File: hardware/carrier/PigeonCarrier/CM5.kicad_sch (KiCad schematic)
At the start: 3 parts, among them J1 10164227-1001A1RLF, J2 10164227-1001A1RLF

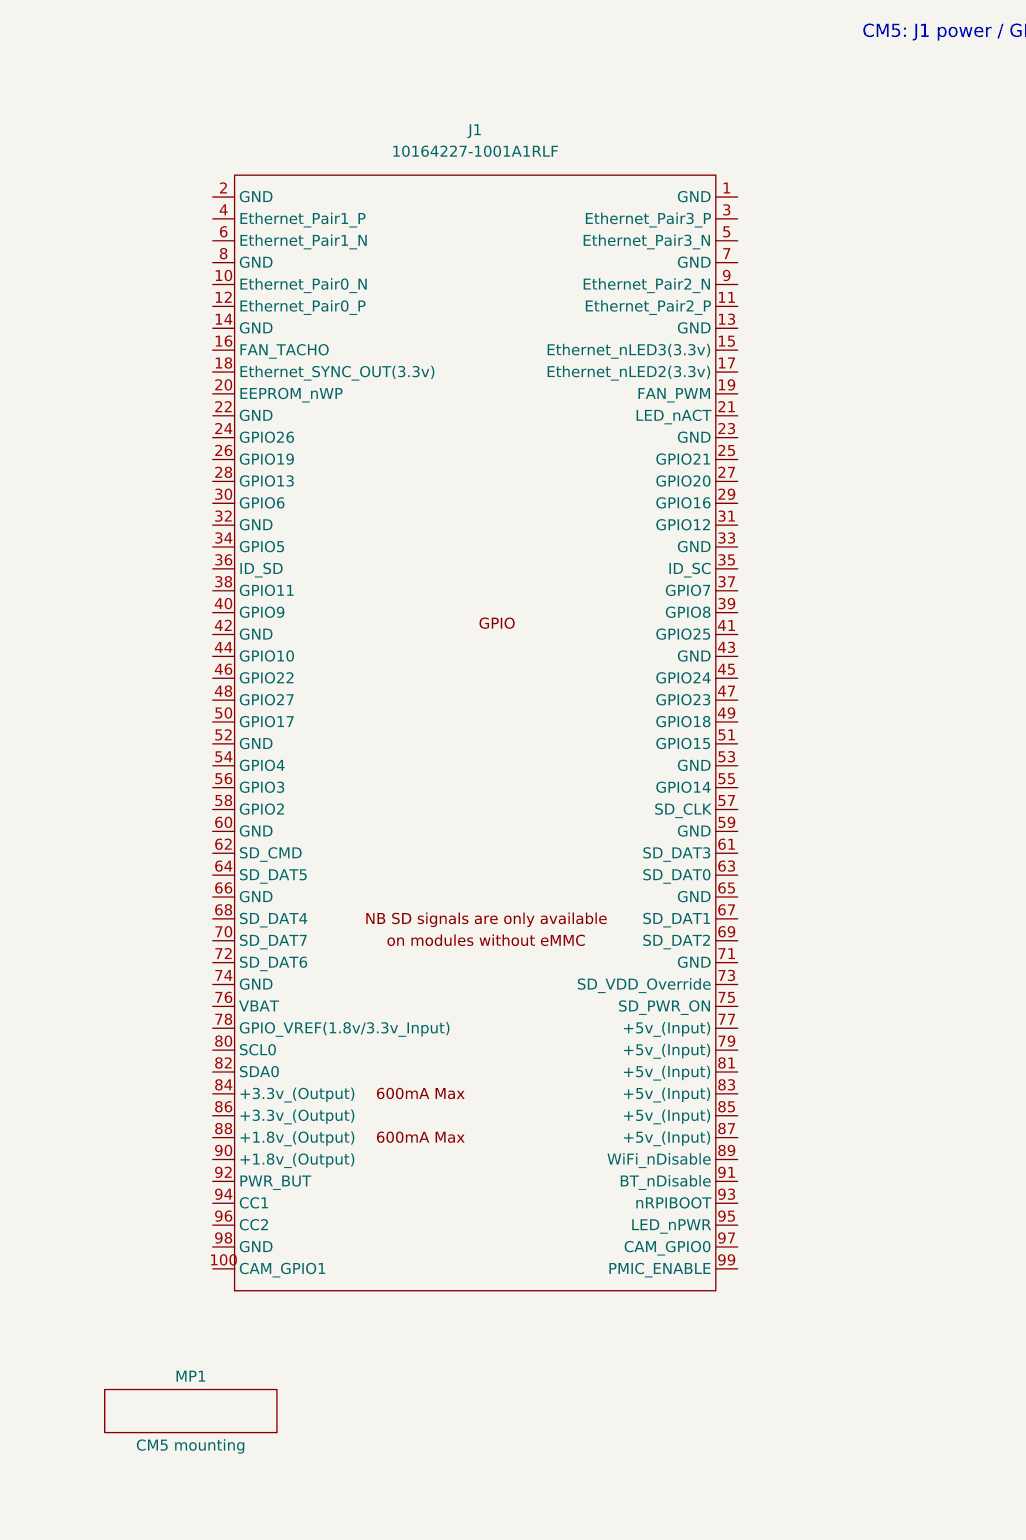
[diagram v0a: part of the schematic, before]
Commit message: shortned readmes + start of power stuff
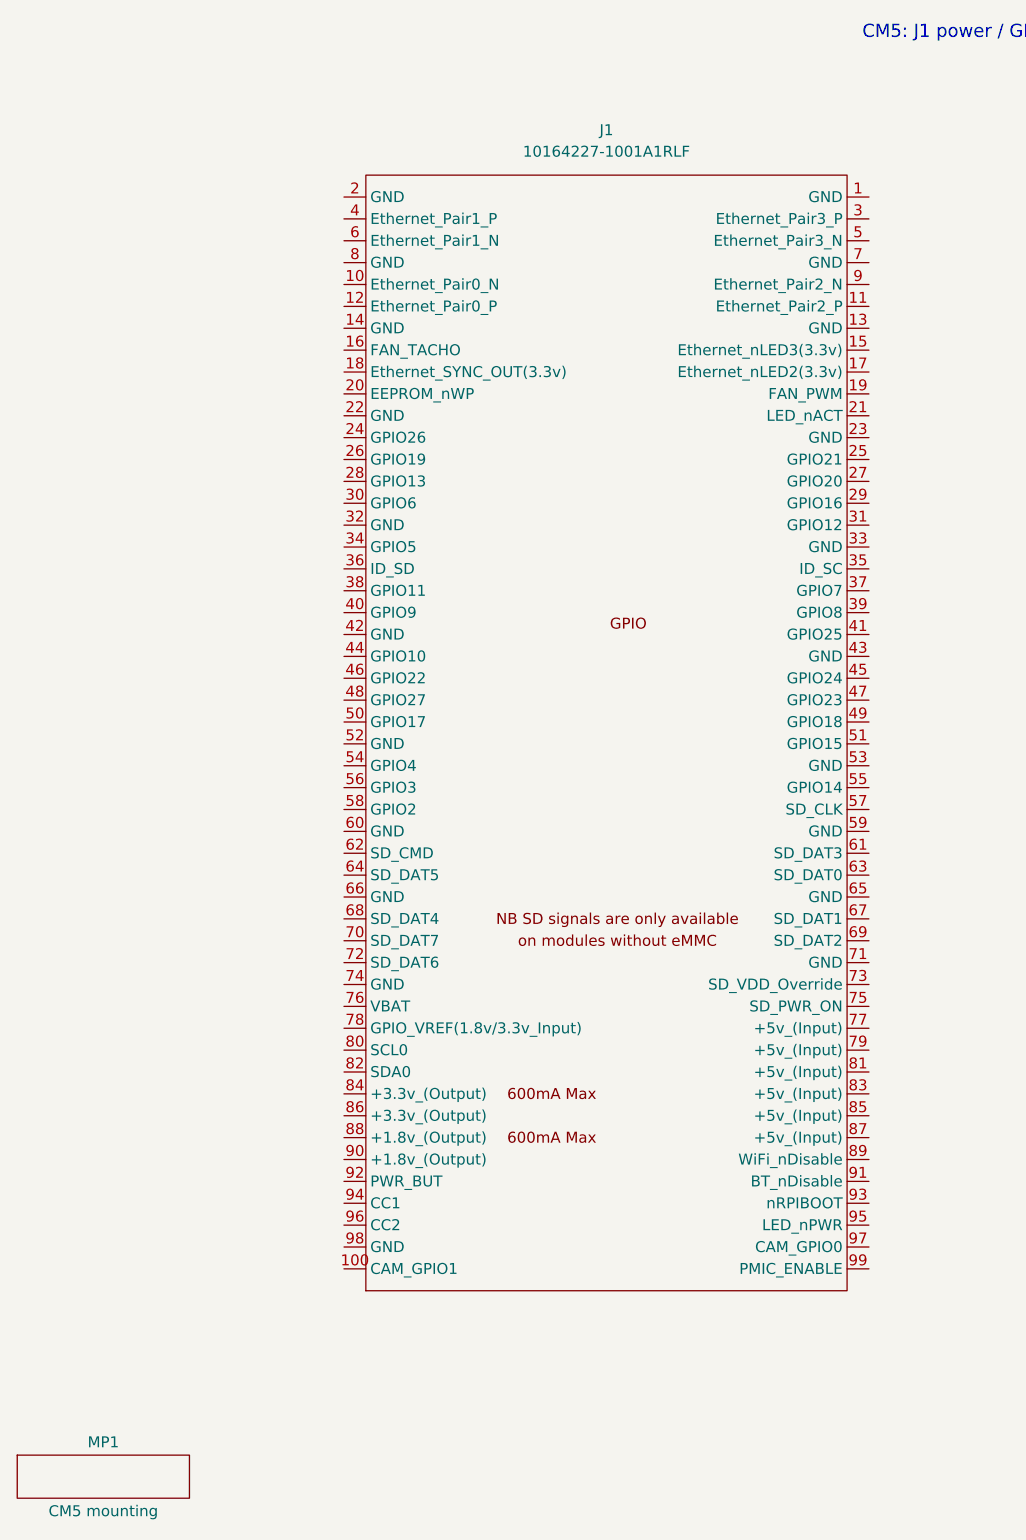
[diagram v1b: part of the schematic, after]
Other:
- moved on the sheet: J1, MP1

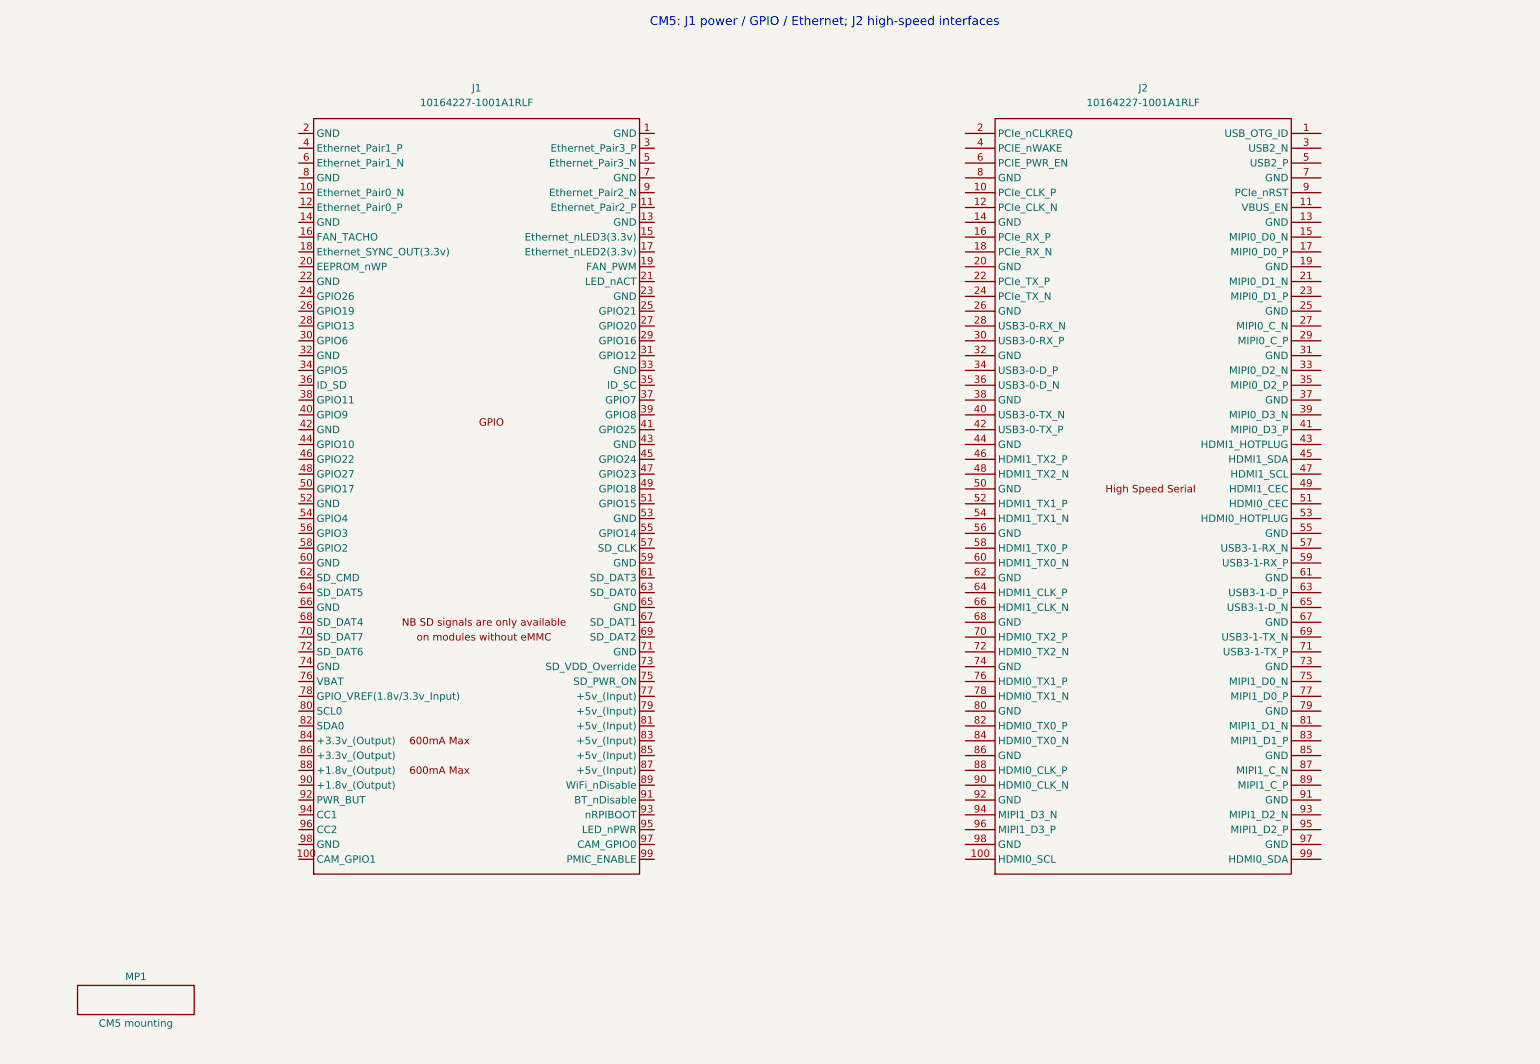
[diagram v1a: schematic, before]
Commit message: Update carrier schematics, parts library, and JLC rules
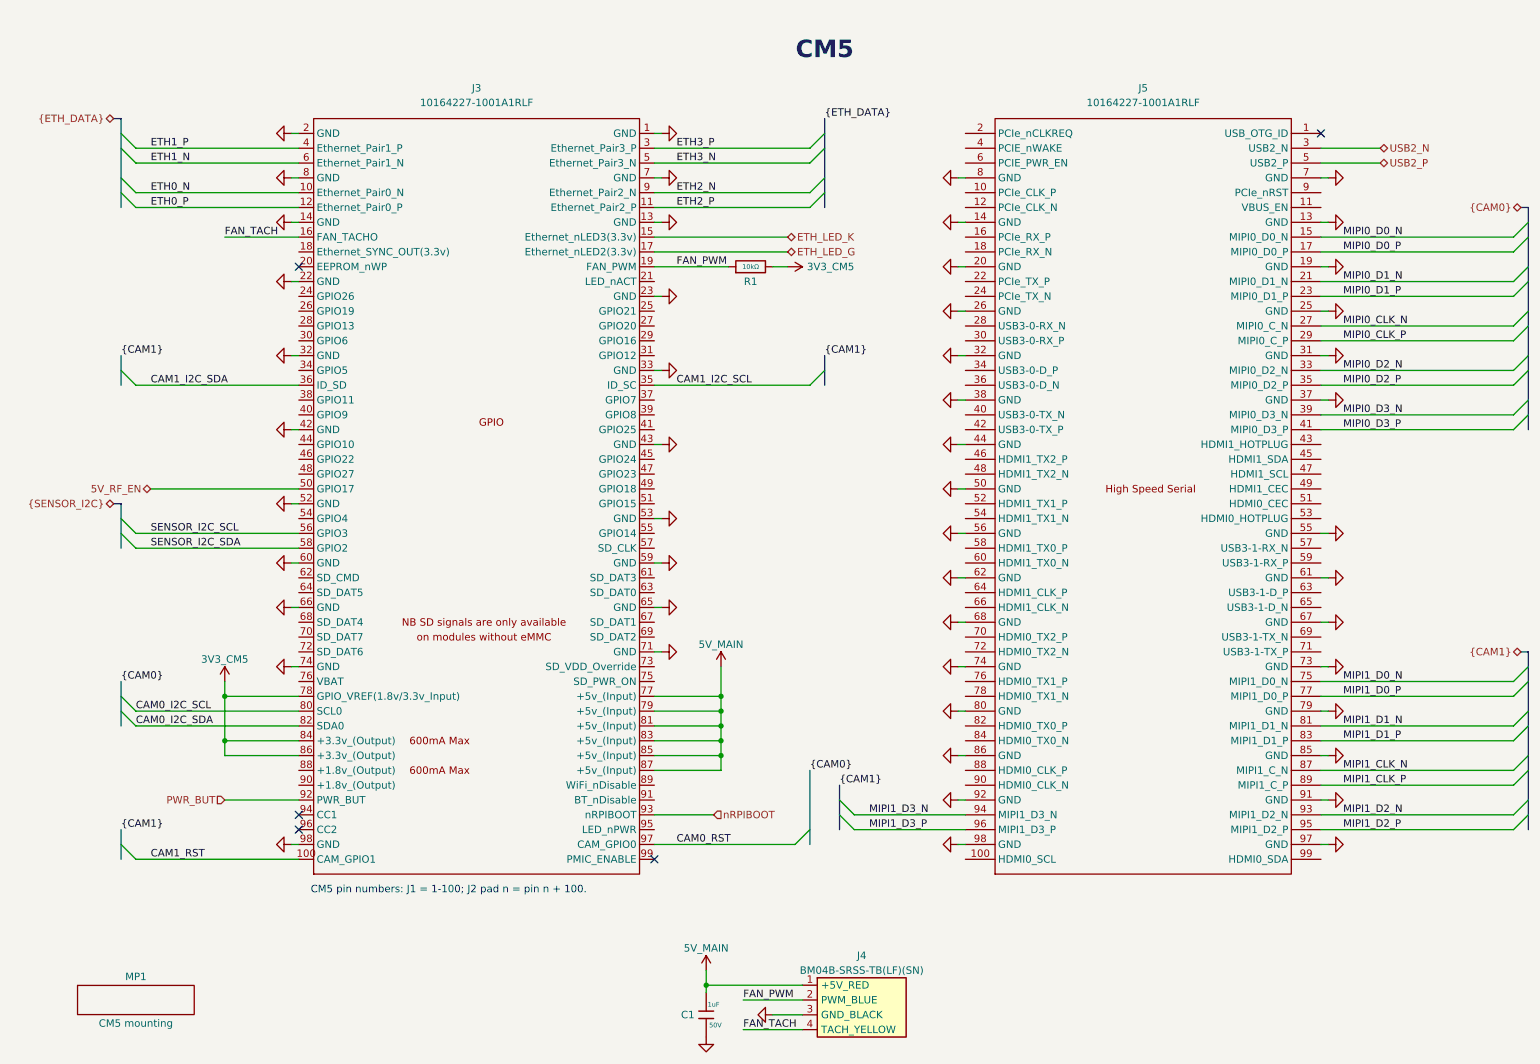
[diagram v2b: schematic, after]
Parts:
- added C1: 1uF, PCM_JLCPCB:C_0805, symbol PCM_JLCPCB-Capacitors:0805,1uF
- added J4: BM04B-SRSS-TB(LF)(SN), PigeonVision:JST_SH_BM04B-SRSS-TB_1x04-1MP_P1.00mm_Vertical, symbol PigeonVision:CM5_Fan_BM04B_SRSS_TB
- added R1: 10kΩ, PCM_JLCPCB:R_0402, symbol PCM_JLCPCB-Resistors:0402,10kΩ
- renumbered J1 to J3, J2 to J5
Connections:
- net GND: now reaches J5.13 (GND)
- net GND: now also J3.1 (GND), J3.13 (GND), J3.14 (GND), J3.2 (GND), J3.22 (GND), J3.23 (GND), J3.32 (GND), J3.33 (GND), J3.42 (GND), J3.43 (GND), J3.52 (GND), J3.53 (GND), J3.59 (GND), J3.60 (GND), J3.65 (GND), J3.66 (GND), J3.7 (GND), J3.71 (GND), J3.74 (GND), J3.8 (GND), J3.98 (GND), J5.14 (GND), J5.19 (GND), J5.20 (GND), J5.25 (GND), J5.26 (GND), J5.31 (GND), J5.32 (GND), J5.37 (GND), J5.38 (GND), J5.44 (GND), J5.50 (GND), J5.55 (GND), J5.56 (GND), J5.61 (GND), J5.62 (GND), J5.67 (GND), J5.68 (GND), J5.7 (GND), J5.73 (GND), J5.74 (GND), J5.79 (GND), J5.8 (GND), J5.80 (GND), J5.85 (GND), J5.86 (GND), J5.91 (GND), J5.92 (GND), J5.97 (GND), J5.98 (GND), C1.2, J4.3 (GND_BLACK)
- net MIPI0_D0_N: now reaches J5.15 (MIPI0_D0_N)
- net MIPI0_D0_P: now reaches J5.17 (MIPI0_D0_P)
- net MIPI0_D1_N: now reaches J5.21 (MIPI0_D1_N)
- net MIPI0_D1_P: now reaches J5.23 (MIPI0_D1_P)
- net MIPI0_CLK_N: now reaches J5.27 (MIPI0_C_N)
- net MIPI0_CLK_P: now reaches J5.29 (MIPI0_C_P)
- net USB2_N: now reaches J5.3 (USB2_N)
- net MIPI0_D2_N: now reaches J5.33 (MIPI0_D2_N)
- net MIPI0_D2_P: now reaches J5.35 (MIPI0_D2_P)
- net MIPI0_D3_N: now reaches J5.39 (MIPI0_D3_N)
- net MIPI0_D3_P: now reaches J5.41 (MIPI0_D3_P)
- net USB2_P: now reaches J5.5 (USB2_P)
- net MIPI1_D0_N: now reaches J5.75 (MIPI1_D0_N)
- net MIPI1_D0_P: now reaches J5.77 (MIPI1_D0_P)
- net MIPI1_D1_N: now reaches J5.81 (MIPI1_D1_N)
- net MIPI1_D1_P: now reaches J5.83 (MIPI1_D1_P)
- net MIPI1_CLK_N: now reaches J5.87 (MIPI1_C_N)
- net MIPI1_CLK_P: now reaches J5.89 (MIPI1_C_P)
- net MIPI1_D2_N: now reaches J5.93 (MIPI1_D2_N)
- net MIPI1_D3_N: now reaches J5.94 (MIPI1_D3_N)
- net MIPI1_D2_P: now reaches J5.95 (MIPI1_D2_P)
- net MIPI1_D3_P: now reaches J5.96 (MIPI1_D3_P)
- net ETH0_N: now reaches J3.10 (Ethernet_Pair0_N)
- net CAM1_RST: now reaches J3.100 (CAM_GPIO1)
- net ETH2_P: now reaches J3.11 (Ethernet_Pair2_P)
- net ETH0_P: now reaches J3.12 (Ethernet_Pair0_P)
- net ETH_LED_K: now reaches J3.15 (Ethernet_nLED3(3.3v))
- net FAN_TACH: now reaches J3.16 (FAN_TACHO)
- net FAN_TACH: now also J4.4 (TACH_YELLOW)
- net ETH_LED_G: now reaches J3.17 (Ethernet_nLED2(3.3v))
- net FAN_PWM: now reaches J3.19 (FAN_PWM)
- net FAN_PWM: now also J4.2 (PWM_BLUE), R1.1
- net ETH3_P: now reaches J3.3 (Ethernet_Pair3_P)
- net CAM1_I2C_SCL: now reaches J3.35 (ID_SC)
- net CAM1_I2C_SDA: now reaches J3.36 (ID_SD)
- net ETH1_P: now reaches J3.4 (Ethernet_Pair1_P)
- net ETH3_N: now reaches J3.5 (Ethernet_Pair3_N)
- net 5V_RF_EN: now reaches J3.50 (GPIO17)
- net SENSOR_I2C_SCL: now reaches J3.56 (GPIO3)
- net SENSOR_I2C_SDA: now reaches J3.58 (GPIO2)
- net ETH1_N: now reaches J3.6 (Ethernet_Pair1_N)
- net 5V_MAIN: now reaches J3.77 (+5v_(Input))
- net 5V_MAIN: now also J3.79 (+5v_(Input)), J3.81 (+5v_(Input)), J3.83 (+5v_(Input)), J3.85 (+5v_(Input)), J3.87 (+5v_(Input)), C1.1, J4.1 (+5V_RED)
- net 3V3_CM5: now reaches J3.78 (GPIO_VREF(1.8v/3.3v_Input))
- net 3V3_CM5: now also J3.84 (+3.3v_(Output)), J3.86 (+3.3v_(Output)), R1.2
- net CAM0_I2C_SCL: now reaches J3.80 (SCL0)
- net CAM0_I2C_SDA: now reaches J3.82 (SDA0)
- net ETH2_N: now reaches J3.9 (Ethernet_Pair2_N)
- net PWR_BUT: now reaches J3.92 (PWR_BUT)
- net nRPIBOOT: now reaches J3.93 (nRPIBOOT)
- net CAM0_RST: now reaches J3.97 (CAM_GPIO0)
- no-connect marks 0 -> 5
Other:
- note added: "CM5"
- note added: "CM5 pin numbers: J1 = 1-100; J2 pad n = pin n + 100."
- note removed: "CM5: J1 power / GPIO / Ethernet; J2 high-speed interfaces"

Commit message: finished rough layout
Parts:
- added J12: UART, PigeonVision:JST_SH_BM03B-SRSS-TB_1x03-1MP_P1.00mm_Vertical, symbol Connector_Generic:Conn_01x03
- added LED4: 0805G_Green, JLCImport_Auto:0805G_Green, symbol JLCImport_Auto:0805G_Green
- added R39, R40: 1kΩ, PCM_JLCPCB:R_0402, symbol PCM_JLCPCB-Resistors:0402,1kΩ
- added R41: 220Ω, PCM_JLCPCB:R_0402, symbol PCM_JLCPCB-Resistors:0402,220Ω
- C1: MPN (none) -> CL21B105KBFNNNE
- R1: MPN (none) -> 0402WGF1002TCE
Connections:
- net 3V3_CM5: now also R41.1
- net GND: now also MP1.1 (H1), MP1.2 (H2), MP1.3 (H3), MP1.4 (H4), J12.2 (Pin_2)
- net LED_nACT: now reaches J3.21 (LED_nACT)
- net LED_nACT: now also LED4.2 (K)
- net UART_RX: now reaches J3.51 (GPIO15)
- net UART_RX: now also R40.1
- net UART_TX: now reaches J3.55 (GPIO14)
- net UART_TX: now also R39.1
- net ETH_LED_K renamed ETH_LED_Y
- new net: LED4.1 (A), R41.2
- new net: J12.1 (Pin_1), R40.2
- new net: J12.3 (Pin_3), R39.2
- no-connect marks 5 -> 92
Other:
- note added: "CM5 activity LED"
- note added: "CM5 connectors: J3 = pins 1-100; J5 pad n = pin n + 100."
- note added: "Debug UART"
- note removed: "CM5 pin numbers: J1 = 1-100; J2 pad n = pin n + 100."
- moved on the sheet: C1, J4
